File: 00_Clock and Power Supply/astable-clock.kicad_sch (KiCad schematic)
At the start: 7 parts, among them U2 LM555xN

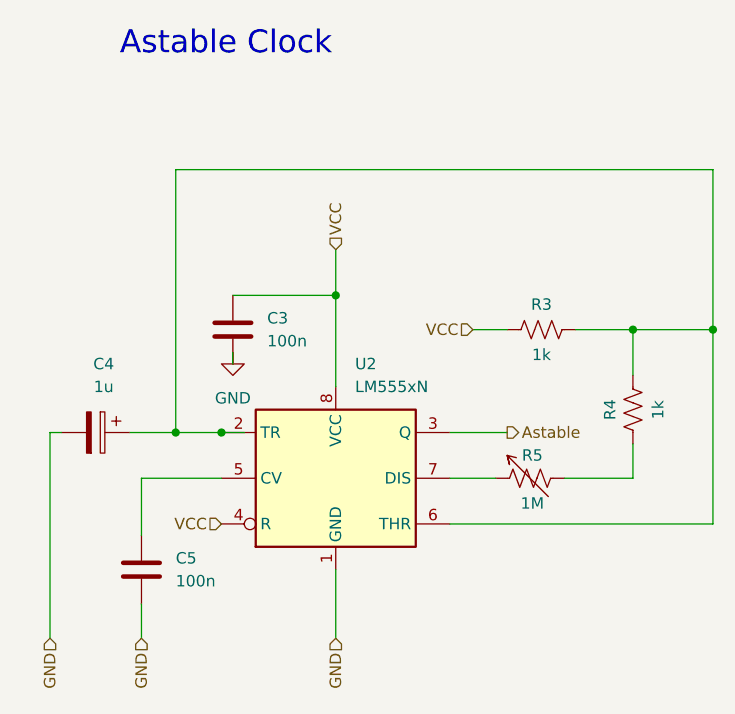
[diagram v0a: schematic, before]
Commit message: Last revision of the cpu, all boards have been ordered. Implementation to be tested and documented in following commits.
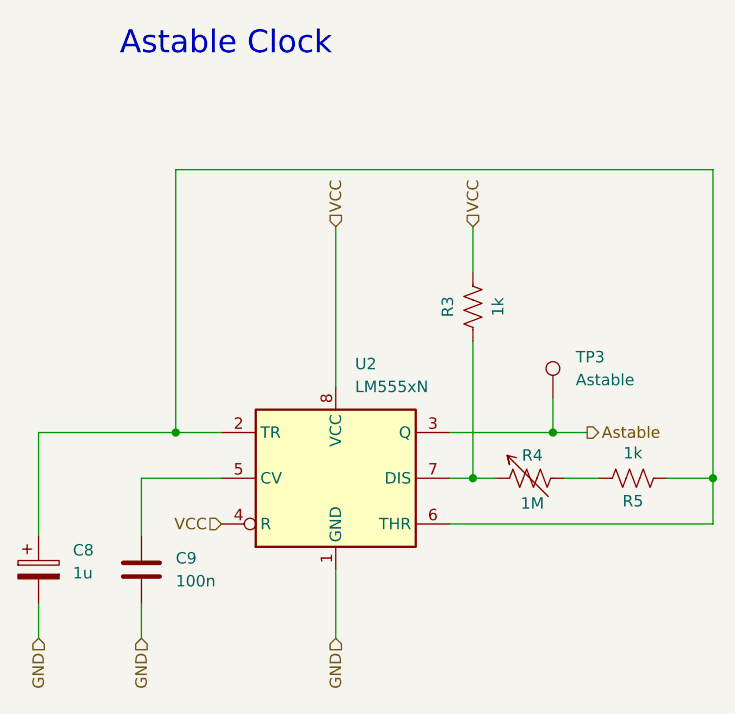
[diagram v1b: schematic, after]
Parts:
- removed C3: 100n, Capacitor_THT:C_Disc_D3.0mm_W1.6mm_P2.50mm, symbol Device:C
- added TP3: Astable, TestPoint:TestPoint_Loop_D3.50mm_Drill0.9mm_Beaded, symbol Connector:TestPoint
- renumbered C4 to C8, C5 to C9, R5 to R4, R4 to R5
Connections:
- net Astable: now also TP3.1
- net VCC: now also R3.2; no longer R3.1
- net at C8.1, U2.2 (TR), U2.6 (THR): now also R5.1; no longer R3.2, R5.2
- net at R4.1, U2.7 (DIS): now also R3.1
- net at R4.2: now also R5.2; no longer R5.1
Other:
- moved on the sheet: C8, R3, R5
